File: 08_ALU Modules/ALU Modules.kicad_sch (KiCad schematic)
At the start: 5 parts, among them J1 Flags, J2 Alu-X Bus, J3 Alu-Y Bus, J4 Alu-Out Bus, J5 Input 1

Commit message: Last revision of the cpu, all boards have been ordered. Implementation to be tested and documented in following commits.
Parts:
- added TP1: VCC, TestPoint:TestPoint_Loop_D3.50mm_Drill0.9mm_Beaded, symbol Connector:TestPoint
- added TP2: GND, TestPoint:TestPoint_Loop_D3.50mm_Drill0.9mm_Beaded, symbol Connector:TestPoint
- added TP3: CLK, TestPoint:TestPoint_Loop_D3.50mm_Drill0.9mm_Beaded, symbol Connector:TestPoint
- renumbered J2 to J1, J3 to J2, J4 to J3, J5 to J4, J1 to J5
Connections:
- net CLK: now also TP3.1
- net GND: now also TP2.1
- net VCC: now also TP1.1
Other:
- note added: "ERC"
- note added: "Test Points"

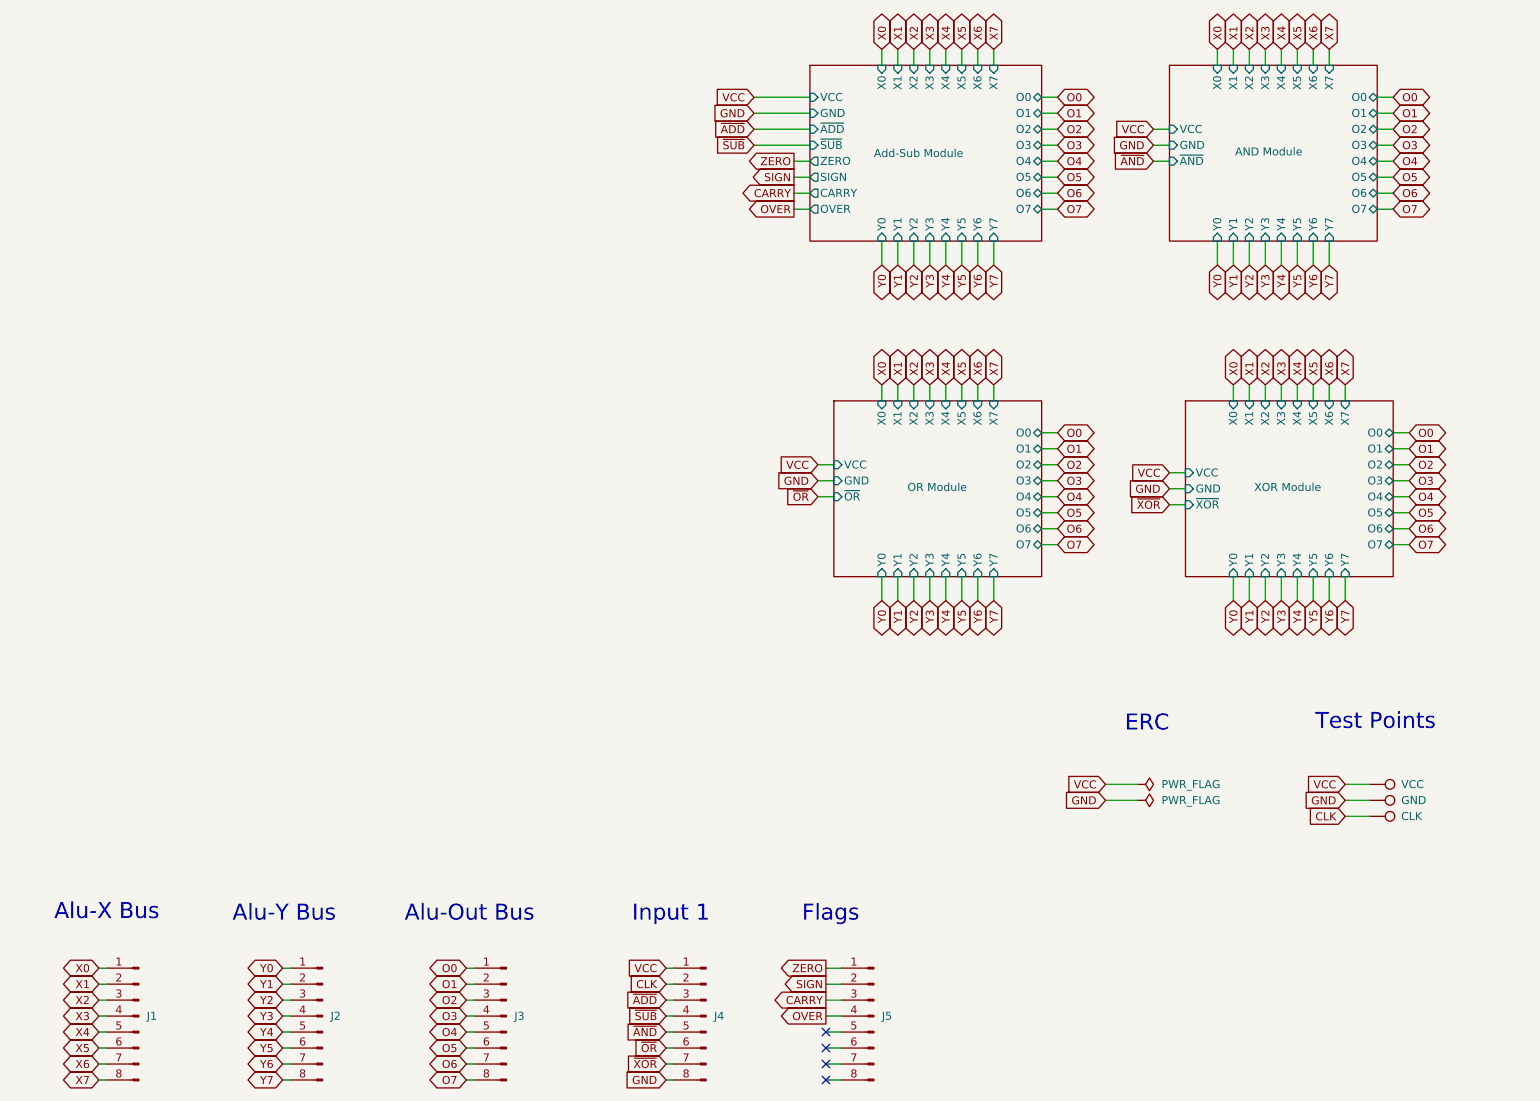
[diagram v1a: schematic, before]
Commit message: Update 10-01-2026 - Fixed bug on program counter - Fist ISA review, still in draft - Added missing mounting holes on memory modules
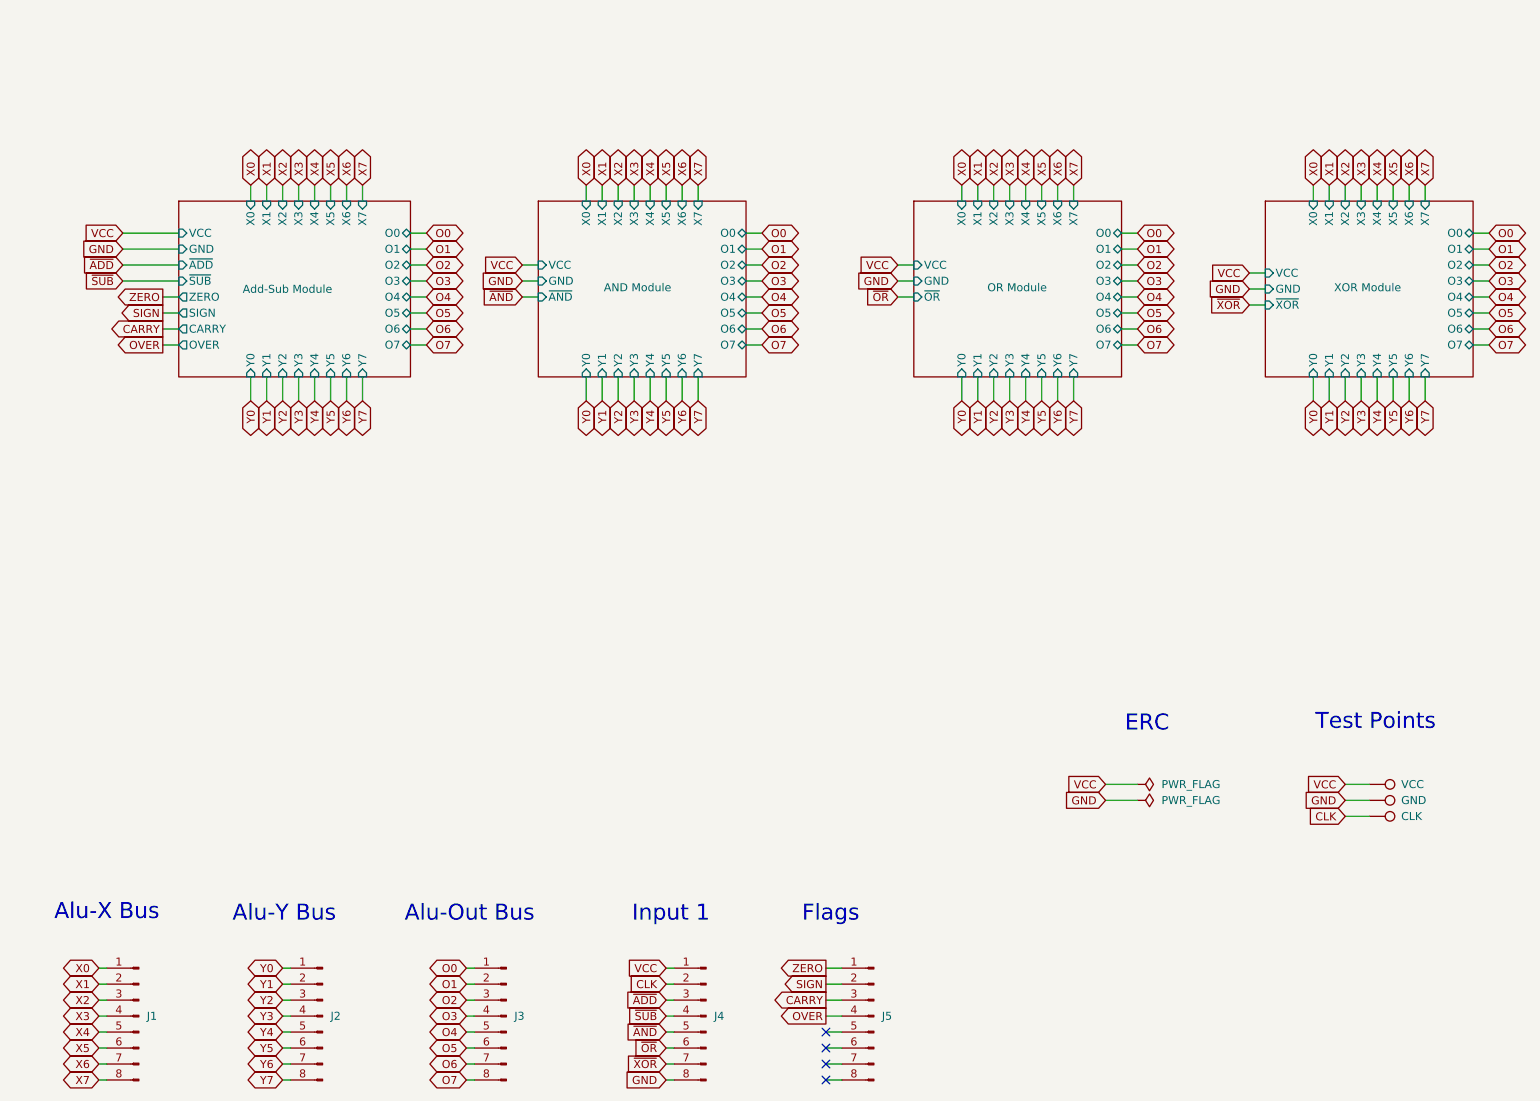
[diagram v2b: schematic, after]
